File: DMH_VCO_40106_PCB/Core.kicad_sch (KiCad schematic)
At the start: 45 parts, among them Q1 BC558, Q2 BC548, U1 40106, U2 TL074

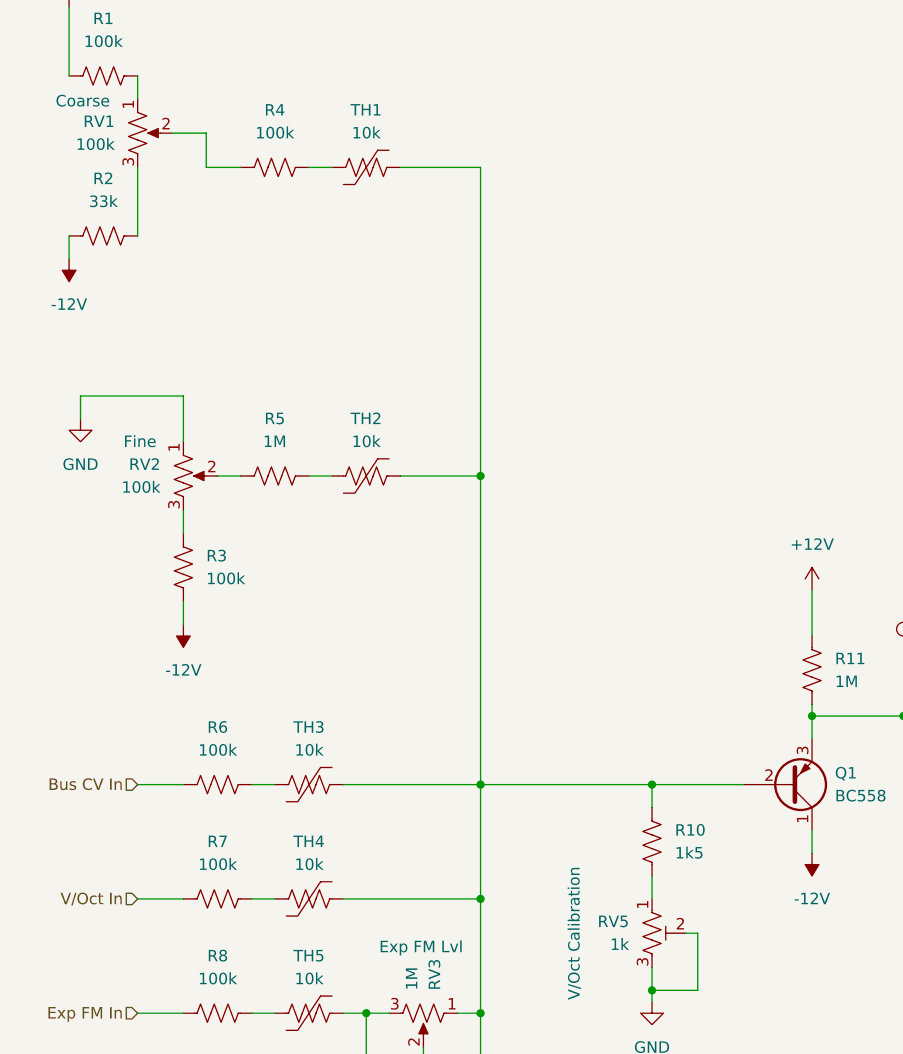
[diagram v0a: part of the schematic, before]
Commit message: Marked components using temporary values
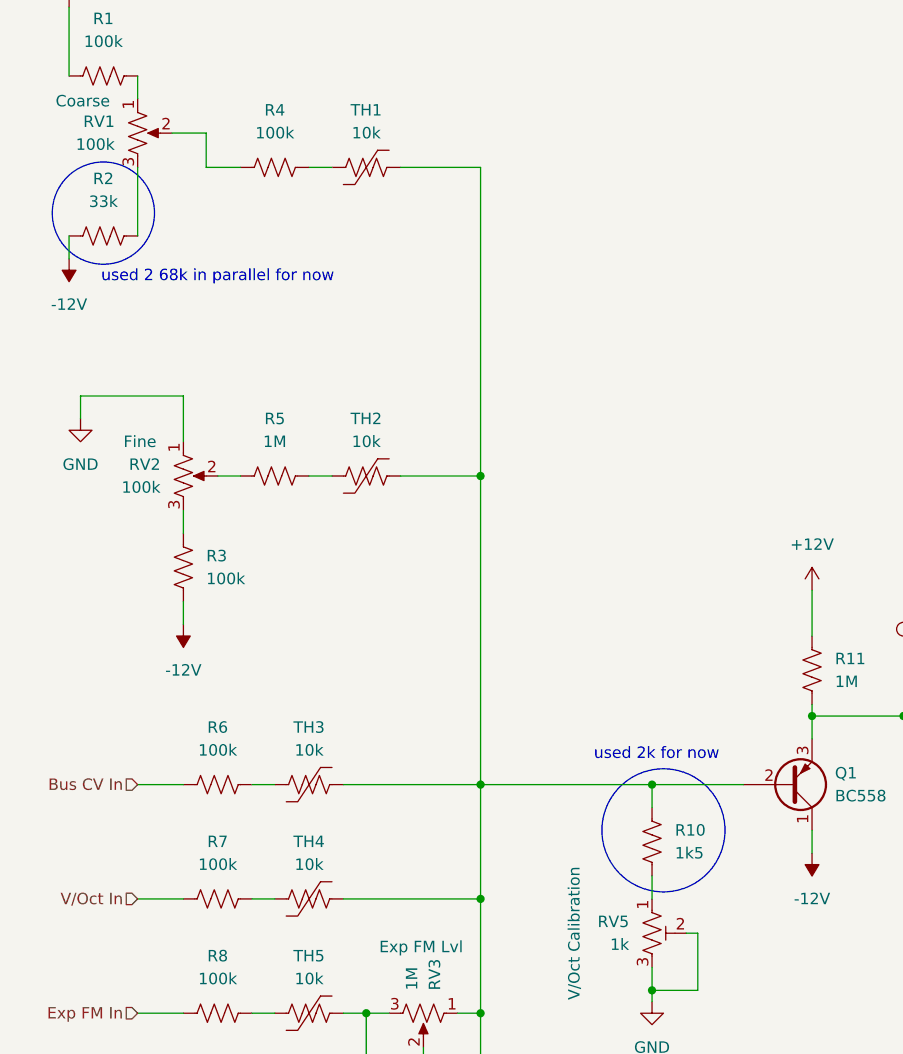
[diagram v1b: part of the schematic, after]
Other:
- note added: "used 2 68k in parallel for now"
- note added: "used 2k for now"
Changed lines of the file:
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@@
+		)
+	)
+	(circle
+		(center 83.82 113.03)
+		(radius 6.8392)
+		(stroke
+			(width 0)
+			(type default)
+		)
+		(fill
+			(type none)
+		)
+	)
+	(circle
+		(center 21.59 44.45)
+		(radius 5.6796)
+		(stroke
+			(width 0)
+			(type default)
+		)
+		(fill
+			(type none)
+		)
+	)
+	(text "used 2k for now"
+		(exclude_from_sim no)
+		(at 83.058 104.648 0)
+		(effects
+			(font
+				(size 1.27 1.27)
+			)
+		)
+	)
+	(text "used 2 68k in parallel for now"
+		(exclude_from_sim no)
+		(at 34.29 51.562 0)
+		(effects
+			(font
+				(size 1.27 1.27)
+			)
 		)
 	)
